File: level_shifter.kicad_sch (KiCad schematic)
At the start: 5 parts, among them U1 TXS0102QDCURQ1

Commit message: Added pcb files for ethernet breakout board
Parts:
- U1: External Part Number (none) -> 595-TXS0102QDCURQ1; MPN (none) -> C2652939
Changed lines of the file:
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@@
+			)
+		)
+		(property "External Part Number" ""
+			(at 181.61 64.77 0)
+			(hide yes)
+			(show_name no)
+			(do_not_autoplace no)
+			(effects
+				(font
+					(size 1.27 1.27)
+				)
+			)
+		)
+		(property "MPN" ""
+			(at 181.61 64.77 0)
+			(hide yes)
+			(show_name no)
+			(do_not_autoplace no)
+			(effects
+				(font
+					(size 1.27 1.27)
+				)
 			)
 		)
@@
 			)
 		)
+		(property "External Part Number" ""
+			(at 167.64 83.82 0)
+			(hide yes)
+			(show_name no)
+			(do_not_autoplace no)
+			(effects
+				(font
+					(size 1.27 1.27)
+				)
+			)
+		)
+		(property "MPN" ""
+			(at 167.64 83.82 0)
+			(hide yes)
+			(show_name no)
+			(do_not_autoplace no)
+			(effects
+				(font
+					(size 1.27 1.27)
+				)
+			)
+		)
 		(pin "2"
 		)
@@
 		)
 		(property "MANUFACTURER_PART_NUMBER" "GCM155R71H104KE02D"
+			(at 170.18 64.77 0)
+			(hide yes)
+			(show_name no)
+			(do_not_autoplace no)
+			(effects
+				(font
+					(size 1.27 1.27)
+				)
+			)
+		)
+		(property "External Part Number" ""
+			(at 170.18 64.77 0)
+			(hide yes)
+			(show_name no)
+			(do_not_autoplace no)
+			(effects
+				(font
+					(size 1.27 1.27)
+				)
+			)
+		)
+		(property "MPN" ""
 			(at 170.18 64.77 0)
 			(hide yes)
@@
 			)
 		)
+		(property "External Part Number" "595-TXS0102QDCURQ1"
+			(at 128.27 72.39 0)
+			(hide yes)
+			(show_name no)
+			(do_not_autoplace no)
+			(effects
+				(font
+					(size 1.27 1.27)
+				)
+			)
+		)
+		(property "MPN" "C2652939"
+			(at 128.27 72.39 0)
+			(hide yes)
+			(show_name no)
+			(do_not_autoplace no)
+			(effects
+				(font
+					(size 1.27 1.27)
+				)
+			)
+		)
 		(pin "8"
 		)
@@
 			(at 124.46 64.77 0)
 			(hide yes)
+			(show_name no)
+			(do_not_autoplace no)
+			(effects
+				(font
+					(size 1.27 1.27)
+				)
+			)
+		)
+		(property "External Part Number" ""
+			(at 124.46 64.77 0)
+			(hide yes)
+			(show_name no)
+			(do_not_autoplace no)
+			(effects
+				(font
+					(size 1.27 1.27)
+				)
+			)
+		)
+		(property "MPN" ""
+			(at 124.46 64.77 0)
+			(hide yes)

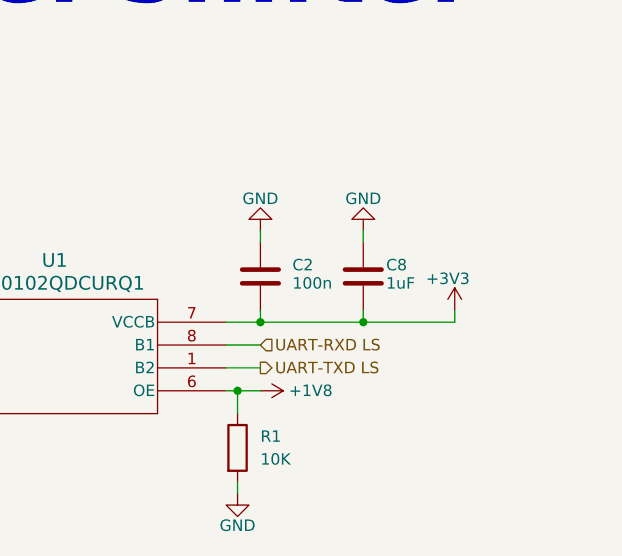
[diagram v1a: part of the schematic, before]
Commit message: Updated BOM and added fiducials
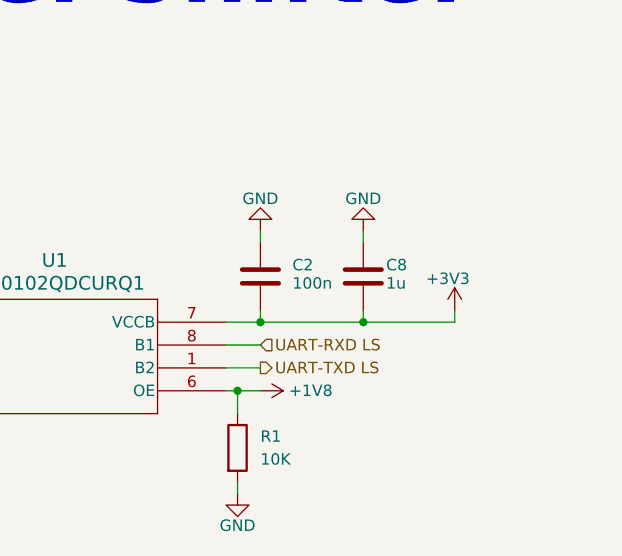
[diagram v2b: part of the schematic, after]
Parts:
- C1, C2: External Part Number (none) -> GCM188R71H104KA57J; MANUFACTURER_PART_NUMBER GCM155R71H104KE02D -> (none); MPN (none) -> C3011652
- C8: value 1uF -> 1u; External Part Number (none) -> GCM188R71E105KA64D; MANUFACTURER_PART_NUMBER GCM155R71H104KE02D -> (none); MPN (none) -> C85862
- R1: External Part Number (none) -> MCS0402MD1002BE100; MANUFACTURER (none) -> Vishay; MPN (none) -> C2073498
- U1: External Part Number 595-TXS0102QDCURQ1 -> TXS0102QDCURQ1; MANUFACTURER_PART_NUMBER TXS0102QDCURQ1 -> (none)
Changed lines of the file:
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@@
 			)
 		)
-		(property "Value" "1uF"
+		(property "Value" "1u"
 			(at 184.15 65.532 0)
 			(show_name no)
@@
 			)
 		)
-		(property "MANUFACTURER_PART_NUMBER" "GCM155R71H104KE02D"
+		(property "External Part Number" "GCM188R71E105KA64D"
 			(at 181.61 64.77 0)
 			(hide yes)
@@
 			)
 		)
-		(property "External Part Number" ""
-			(at 181.61 64.77 0)
-			(hide yes)
-			(show_name no)
-			(do_not_autoplace no)
-			(effects
-				(font
-					(size 1.27 1.27)
-				)
-			)
-		)
-		(property "MPN" ""
+		(property "MPN" "C85862"
 			(at 181.61 64.77 0)
 			(hide yes)
@@
 			)
 		)
-		(property "External Part Number" ""
+		(property "External Part Number" "MCS0402MD1002BE100"
 			(at 167.64 83.82 0)
 			(hide yes)
@@
 			)
 		)
-		(property "MPN" ""
+		(property "MPN" "C2073498"
+			(at 167.64 83.82 0)
+			(hide yes)
+			(show_name no)
+			(do_not_autoplace no)
+			(effects
+				(font
+					(size 1.27 1.27)
+				)
+			)
+		)
+		(property "MANUFACTURER" "Vishay"
 			(at 167.64 83.82 0)
 			(hide yes)
@@
 			)
 		)
-		(property "MANUFACTURER_PART_NUMBER" "GCM155R71H104KE02D"
+		(property "External Part Number" "GCM188R71H104KA57J"
 			(at 170.18 64.77 0)
 			(hide yes)
@@
 			)
 		)
-		(property "External Part Number" ""
-			(at 170.18 64.77 0)
-			(hide yes)
-			(show_name no)
-			(do_not_autoplace no)
-			(effects
-				(font
-					(size 1.27 1.27)
-				)
-			)
-		)
-		(property "MPN" ""
+		(property "MPN" "C3011652"
 			(at 170.18 64.77 0)
 			(hide yes)
@@
 			)
 		)
-		(property "MANUFACTURER_PART_NUMBER" "TXS0102QDCURQ1"
-			(at 128.27 72.39 0)
-			(hide yes)
-			(show_name no)
-			(do_not_autoplace no)
-			(effects
-				(font
-					(size 1.27 1.27)
-				)
-			)
-		)
 		(property "MANUFACTURER" "  Texas Instruments"
 			(at 128.27 72.39 0)
@@
 			)
 		)
-		(property "External Part Number" "595-TXS0102QDCURQ1"
+		(property "External Part Number" "TXS0102QDCURQ1"
 			(at 128.27 72.39 0)
 			(hide yes)
@@
 			)
 		)
-		(property "MANUFACTURER_PART_NUMBER" "GCM155R71H104KE02D"
+		(property "External Part Number" "GCM188R71H104KA57J"
 			(at 124.46 64.77 0)
 			(hide yes)
@@
 			)
 		)
-		(property "External Part Number" ""
+		(property "MPN" "C3011652"
 			(at 124.46 64.77 0)
 			(hide yes)
-			(show_name no)
-			(do_not_autoplace no)
-			(effects
-				(font
-					(size 1.27 1.27)
-				)
-			)
-		)
-		(property "MPN" ""
-			(at 124.46 64.77 0)
-			(hide yes)

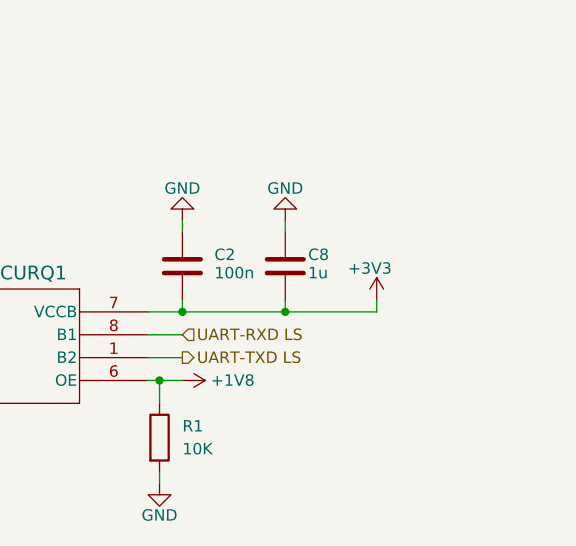
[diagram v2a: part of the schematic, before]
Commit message: Changed connector orientation and power changes
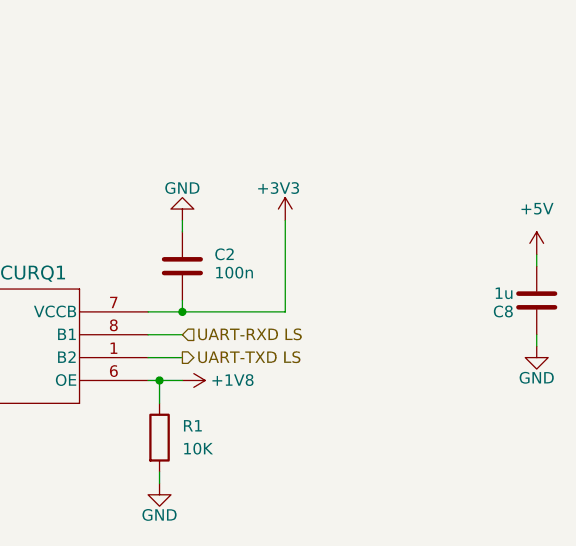
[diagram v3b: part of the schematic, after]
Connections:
- net +3V3: no longer C8.2
- new net +5V: C8.2
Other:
- moved on the sheet: C8
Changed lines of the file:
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@@
 		(color 0 0 0 0)
 	)
-	(junction
-		(at 181.61 69.85)
-		(diameter 0)
-		(color 0 0 0 0)
-	)
 	(wire
 		(pts
@@
 	(wire
 		(pts
-			(xy 181.61 59.69) (xy 181.61 60.96)
-		)
-		(stroke
-			(width 0)
-			(type default)
-		)
-	)
-	(wire
-		(pts
 			(xy 125.73 80.01) (xy 125.73 77.47)
 		)
@@
 	(wire
 		(pts
-			(xy 181.61 69.85) (xy 191.77 69.85)
-		)
-		(stroke
-			(width 0)
-			(type default)
-		)
-	)
-	(wire
-		(pts
 			(xy 107.95 67.31) (xy 107.95 69.85)
 		)
@@
 	(wire
 		(pts
-			(xy 181.61 68.58) (xy 181.61 69.85)
+			(xy 209.55 73.66) (xy 209.55 72.39)
+		)
+		(stroke
+			(width 0)
+			(type default)
+		)
+	)
+	(wire
+		(pts
+			(xy 209.55 63.5) (xy 209.55 64.77)
 		)
 		(stroke
@@
 	(wire
 		(pts
-			(xy 191.77 69.85) (xy 191.77 68.58)
+			(xy 181.61 69.85) (xy 181.61 59.69)
 		)
 		(stroke
@@
 	(symbol
 		(lib_id "Device:C")
-		(at 181.61 64.77 0)
+		(at 209.55 68.58 180)
 		(unit 1)
 		(body_style 1)
@@
 		(dnp no)
 		(property "Reference" "C8"
-			(at 184.15 63.5 0)
+			(at 207.01 69.85 0)
 			(show_name no)
 			(do_not_autoplace no)
@@
 		)
 		(property "Value" "1u"
-			(at 184.15 65.532 0)
+			(at 207.01 67.818 0)
 			(show_name no)
 			(do_not_autoplace no)
@@
 		)
 		(property "Footprint" "Capacitor_SMD:C_0603_1608Metric"
-			(at 182.5752 68.58 0)
+			(at 208.5848 64.77 0)
 			(hide yes)
 			(show_name no)
@@
 		)
 		(property "Datasheet" ""
-			(at 181.61 64.77 0)
+			(at 209.55 68.58 0)
 			(hide yes)
 			(show_name no)
@@
 		)
 		(property "Description" ""
-			(at 181.61 64.77 0)
+			(at 209.55 68.58 0)
 			(hide yes)
 			(show_name no)
@@
 		)
 		(property "MANUFACTURER" "Murata Electronics"
-			(at 181.61 64.77 0)
+			(at 209.55 68.58 0)
 			(hide yes)
 			(show_name no)
@@
 		)
 		(property "External Part Number" "GCM188R71E105KA64D"
-			(at 181.61 64.77 0)
+			(at 209.55 68.58 0)
 			(hide yes)
 			(show_name no)
@@
 		)
 		(property "MPN" "C85862"
-			(at 181.61 64.77 0)
+			(at 209.55 68.58 0)
 			(hide yes)
 			(show_name no)
@@
 	(symbol
 		(lib_id "power:GND")
-		(at 181.61 59.69 180)
+		(at 209.55 73.66 0)
 		(unit 1)
 		(body_style 1)
@@
 		(dnp no)
 		(property "Reference" "#PWR047"
-			(at 181.61 53.34 0)
+			(at 209.55 80.01 0)
 			(hide yes)
 			(show_name no)
@@
 		)
 		(property "Value" "GND"
-			(at 181.61 56.134 0)
+			(at 209.55 77.216 0)
 			(show_name no)
 			(do_not_autoplace no)
@@
 		)
 		(property "Footprint" ""
-			(at 181.61 59.69 0)
+			(at 209.55 73.66 0)
 			(hide yes)
 			(show_name no)
@@
 		)
 		(property "Datasheet" ""
-			(at 181.61 59.69 0)
+			(at 209.55 73.66 0)
 			(hide yes)
 			(show_name no)
@@
 		)
 		(property "Description" "Power symbol creates a global label with name \"GND\" , ground"
-			(at 181.61 59.69 0)
+			(at 209.55 73.66 0)
 			(hide yes)
 			(show_name no)
@@
 	(symbol
 		(lib_id "power:+3V3")
-		(at 191.77 68.58 0)
+		(at 181.61 59.69 0)
 		(unit 1)
 		(body_style 1)
@@
 		(dnp no)
 		(property "Reference" "#PWR037"
-			(at 191.77 72.39 0)
+			(at 181.61 63.5 0)
 			(hide yes)
 			(show_name no)
@@
 		)
 		(property "Value" "+3V3"
-			(at 191.008 65.024 0)
+			(at 180.848 56.134 0)
 			(show_name no)
 			(do_not_autoplace no)
@@
 		)
 		(property "Footprint" ""
-			(at 191.77 68.58 0)
+			(at 181.61 59.69 0)
 			(hide yes)
 			(show_name no)
@@
 		)
 		(property "Datasheet" ""
-			(at 191.77 68.58 0)
+			(at 181.61 59.69 0)
 			(hide yes)
 			(show_name no)
@@
 		)
 		(property "Description" "Power symbol creates a global label with name \"+3V3\""
-			(at 191.77 68.58 0)
+			(at 181.61 59.69 0)
 			(hide yes)
 			(show_name no)
@@
 					(unit 1)
 				)
+			)
+		)
+	)
+	(symbol
+		(lib_id "power:+5V")
+		(at 209.55 63.5 0)
+		(unit 1)
+		(body_style 1)
+		(exclude_from_sim no)
+		(in_bom yes)
+		(on_board yes)
+		(in_pos_files yes)
+		(dnp no)
+		(fields_autoplaced yes)
+		(property "Reference" "#PWR052"
+			(at 209.55 67.31 0)
+			(hide yes)
+			(show_name no)
+			(do_not_autoplace no)
+			(effects
+				(font
+					(size 1.27 1.27)
+				)
+			)
+		)
+		(property "Value" "+5V"
+			(at 209.55 58.42 0)
+			(show_name no)
+			(do_not_autoplace no)
+			(effects
+				(font
+					(size 1.27 1.27)
+				)
+			)
+		)
+		(property "Footprint" ""
+			(at 209.55 63.5 0)
+			(hide yes)
+			(show_name no)
+			(do_not_autoplace no)
+			(effects
+				(font
+					(size 1.27 1.27)
+				)
+			)
+		)
+		(property "Datasheet" ""
+			(at 209.55 63.5 0)
+			(hide yes)
+			(show_name no)
+			(do_not_autoplace no)
+			(effects
+				(font
+					(size 1.27 1.27)
+				)
+			)
+		)
+		(property "Description" "Power symbol creates a global label with name \"+5V\""
+			(at 209.55 63.5 0)
+			(hide yes)
+			(show_name no)
+			(do_not_autoplace no)
+			(effects
+				(font
+					(size 1.27 1.27)
+				)
+			)
+		)
+		(pin "1"
+		)
+		(instances
+			(project "adapter-pcb"
+				(path "/94da9b83-1146-4f01-8e34-8153765b0257/cf109836-ab8e-48e3-a0ed-36c6666f071e"
+					(reference "#PWR052")
+					(unit 1)
+				)

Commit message: Made very tiny tweaks
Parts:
- U1: MANUFACTURER Texas Instruments -> Texas Instruments
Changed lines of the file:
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@@
 			)
 		)
-		(property "MANUFACTURER" "  Texas Instruments"
+		(property "MANUFACTURER" "Texas Instruments"
 			(at 128.27 72.39 0)
 			(hide yes)

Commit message: added solder bridges and updated BOM
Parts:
- C1, C2: External Part Num (none) -> C3011652; External Part Number GCM188R71H104KA57J -> (none); MPN C3011652 -> GCM188R71H104KA57J
- C8: External Part Num (none) -> C85862; External Part Number GCM188R71E105KA64D -> (none); MPN C85862 -> GCM188R71E105KA64D
- R1: External Part Num (none) -> C2073498; External Part Number MCS0402MD1002BE100 -> (none); MPN C2073498 -> MCS0402MD1002BE100
- U1: External Part Num (none) -> C2652939; External Part Number TXS0102QDCURQ1 -> (none); MPN C2652939 -> TXS0102QDCURQ1
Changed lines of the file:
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@@
 			)
 		)
-		(property "External Part Number" "GCM188R71E105KA64D"
+		(property "MPN" "GCM188R71E105KA64D"
 			(at 209.55 68.58 0)
 			(hide yes)
@@
 			)
 		)
-		(property "MPN" "C85862"
+		(property "External Part Num" "C85862"
 			(at 209.55 68.58 0)
 			(hide yes)
@@
 			)
 		)
-		(property "External Part Number" "MCS0402MD1002BE100"
+		(property "MPN" "MCS0402MD1002BE100"
 			(at 167.64 83.82 0)
 			(hide yes)
@@
 			)
 		)
-		(property "MPN" "C2073498"
+		(property "MANUFACTURER" "Vishay"
 			(at 167.64 83.82 0)
 			(hide yes)
@@
 			)
 		)
-		(property "MANUFACTURER" "Vishay"
+		(property "External Part Num" "C2073498"
 			(at 167.64 83.82 0)
 			(hide yes)
@@
 			)
 		)
-		(property "External Part Number" "GCM188R71H104KA57J"
+		(property "MPN" "GCM188R71H104KA57J"
 			(at 170.18 64.77 0)
 			(hide yes)
@@
 			)
 		)
-		(property "MPN" "C3011652"
+		(property "External Part Num" "C3011652"
 			(at 170.18 64.77 0)
 			(hide yes)
@@
 			)
 		)
-		(property "External Part Number" "TXS0102QDCURQ1"
+		(property "MPN" "TXS0102QDCURQ1"
 			(at 128.27 72.39 0)
 			(hide yes)
@@
 			)
 		)
-		(property "MPN" "C2652939"
+		(property "External Part Num" "C2652939"
 			(at 128.27 72.39 0)
 			(hide yes)
@@
 			)
 		)
-		(property "External Part Number" "GCM188R71H104KA57J"
+		(property "MPN" "GCM188R71H104KA57J"
 			(at 124.46 64.77 0)
 			(hide yes)
@@
 			)
 		)
-		(property "MPN" "C3011652"
+		(property "External Part Num" "C3011652"
 			(at 124.46 64.77 0)
 			(hide yes)
